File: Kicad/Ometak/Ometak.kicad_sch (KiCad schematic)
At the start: 26 parts, among them J1 Conn_01x02_Pin, J2 Conn_01x02_Pin, J3 Conn_01x02_Pin, Q1 IRF7303, U1 L7805, U2 PIC16F15214-I/SN, U3 LM358

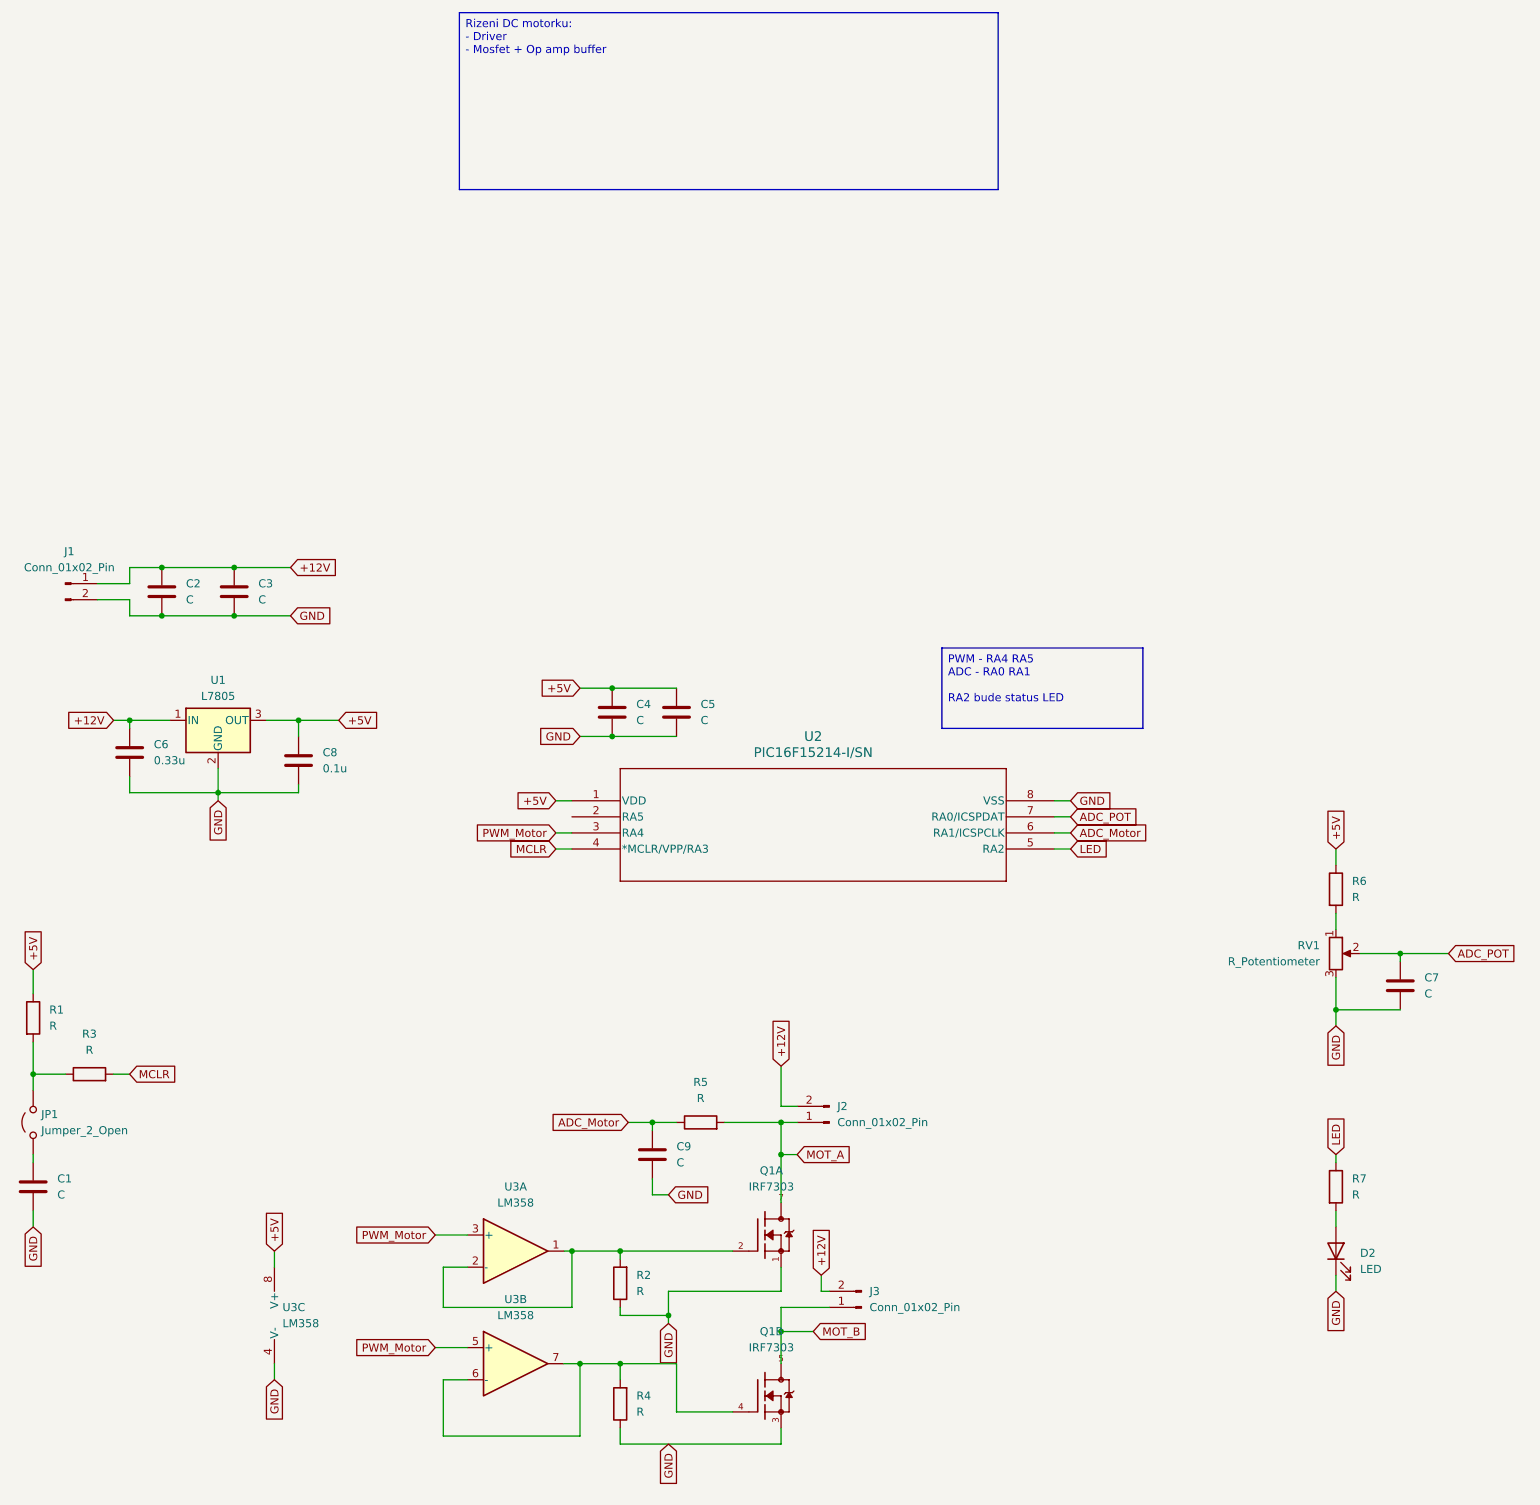
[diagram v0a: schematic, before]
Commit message: Pokrocilejsi verze ometaku - navrh
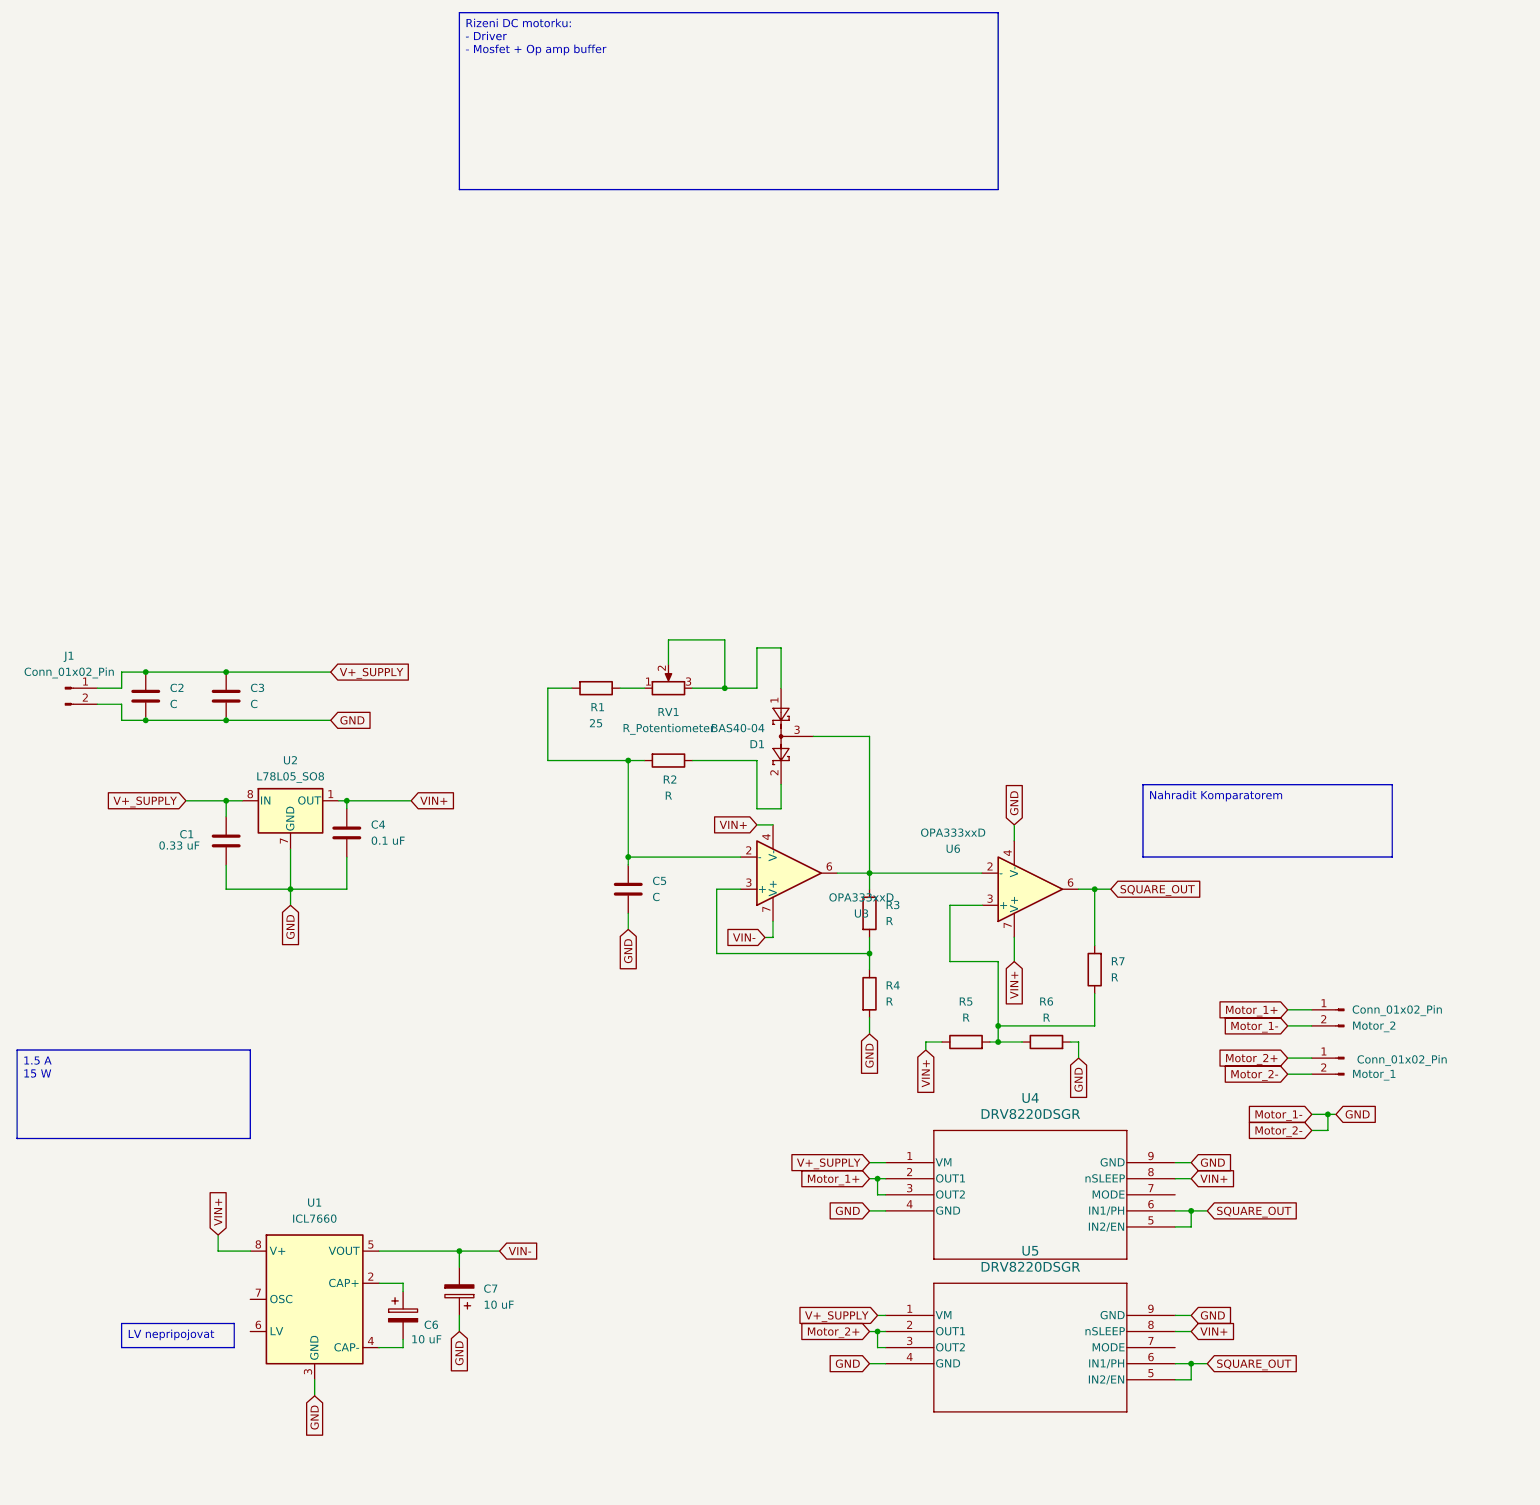
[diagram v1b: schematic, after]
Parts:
- removed C6: 0.33u, Capacitor_SMD:C_1206_3216Metric, symbol Device:C
- removed C7: C, Capacitor_SMD:C_0603_1608Metric, symbol Device:C
- removed C8: 0.1u, Capacitor_SMD:C_1206_3216Metric, symbol Device:C
- removed C9: C, symbol Device:C
- removed D2: LED, LED_SMD:LED_0603_1608Metric, symbol Device:LED
- removed J2, J3: Conn_01x02_Pin, Connector_PinHeader_2.54mm:PinHeader_1x02_P2.54mm_Vertical, symbol Connector:Conn_01x02_Pin
- removed JP1: Jumper_2_Open, Connector_PinHeader_1.27mm:PinHeader_1x02_P1.27mm_Vertical, symbol Jumper:Jumper_2_Open
- removed Q1: IRF7303, IRF7303:SOIC-8, symbol IRF7303:IRF7303
- removed U1: L7805, Package_TO_SOT_SMD:TO-252-2, symbol Regulator_Linear:L7805
- removed U2: PIC16F15214-I/SN, PIC16F15214:SOIC8_SN_MCH, symbol PIC16F15214:PIC16F15214-I_SN
- removed U3: LM358, Package_SO:SOIC-8_3.9x4.9mm_P1.27mm, symbol Amplifier_Operational:LM358
- added C6, C7: 10 uF, Capacitor_SMD:C_1206_3216Metric, symbol Device:C_Polarized
- added D1: BAS40-04, Package_TO_SOT_SMD:SOT-23, symbol Diode:BAS40-04
- added Motor_1, Motor_2: Conn_01x02_Pin, TerminalBlock:TerminalBlock_MaiXu_MX126-5.0-02P_1x02_P5.00mm, symbol Connector:Conn_01x02_Pin
- added U1: ICL7660, Package_SO:SOIC-8_3.9x4.9mm_P1.27mm, symbol Regulator_SwitchedCapacitor:ICL7660
- added U2: L78L05_SO8, Package_SO:SOIC-8_3.9x4.9mm_P1.27mm, symbol Regulator_Linear:L78L05_SO8
- added U3, U6: OPA333xxD, Package_SO:SOIC-8_3.9x4.9mm_P1.27mm, symbol Amplifier_Operational:OPA333xxD
- added U4, U5: DRV8220DSGR, WSON8_DSG_TEX, symbol DRV8220:DRV8220DSGR
- C1: value C -> 0.33 uF; footprint Capacitor_SMD:C_0603_1608Metric -> Capacitor_SMD:C_1206_3216Metric
- C2, C3: footprint Capacitor_THT:CP_Radial_D10.0mm_P2.50mm -> Capacitor_THT:CP_Radial_D10.0mm_P5.00mm
- C4: value C -> 0.1 uF; footprint Capacitor_SMD:C_0603_1608Metric -> Capacitor_SMD:C_1206_3216Metric
- C5: footprint Capacitor_SMD:C_0603_1608Metric -> Capacitor_SMD:C_1206_3216Metric
- J1: footprint Connector_PinHeader_2.54mm:PinHeader_1x02_P2.54mm_Vertical -> TerminalBlock:TerminalBlock_MaiXu_MX126-5.0-02P_1x02_P5.00mm
- R1: value R -> 25; footprint Resistor_SMD:R_0603_1608Metric -> Resistor_SMD:R_1206_3216Metric
- R3, R7: footprint Resistor_SMD:R_0603_1608Metric -> Resistor_SMD:R_1206_3216Metric
- R5: footprint (none) -> Resistor_SMD:R_1206_3216Metric
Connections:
- net +12V is gone; now on net V+_SUPPLY: C2.1, C3.1, J1.1 (Pin_1)
- net MOT_A is gone; now on an unnamed net: R5.2
- net GND: now also R4.2, R6.2, C7.1, Motor_1.2 (Pin_2), Motor_2.2 (Pin_2), U1.3 (GND), U2.2 (GND), U2.3 (GND), U2.6 (GND), U2.7 (GND), U4.4 (GND), U4.9 (GND), U5.4 (GND), U5.9 (GND), U6.4 (V-); no longer R2.1, R4.1, RV1.3
- net at R2.2: now also C5.1, R1.2, U3.2 (-)
- net at RV1.1: now also R1.1; no longer R6.2
- net V+_SUPPLY: now reaches C1.1
- net V+_SUPPLY: now also U2.8 (IN), U4.1 (VM), U5.1 (VM)
- net at R3.1: now also D1.3, U3.6, U6.2 (-); no longer R1.2
- net SQUARE_OUT: now reaches R7.2
- net SQUARE_OUT: now also U4.5 (IN2/EN), U4.6 (IN1/PH), U5.5 (IN2/EN), U5.6 (IN1/PH), U6.6
- removed net +5V: C4.1, C5.1, R1.1, R6.1
- net ADC_Motor renamed VIN+
- net VIN+: now also C4.1, U1.8 (V+), U2.1 (OUT), U3.4 (V-), U4.8 (nSLEEP), U5.8 (nSLEEP), U6.7 (V+)
- net ADC_POT: no longer names the net of RV1.2
- net ADC_POT: now also RV1.3, D1.1
- net LED: no longer names the net of R7.1
- net LED: now also R6.1, U6.3 (+)
- net MCLR: no longer names the net of R3.2
- net MCLR: now also R4.1, U3.3 (+)
- new net: D1.2, R2.1
- new net: C6.1, U1.2 (CAP+)
- new net: C6.2, U1.4 (CAP-)
- new net Motor_1+: Motor_2.1 (Pin_1), U4.2 (OUT1), U4.3 (OUT2)
- new net Motor_2+: Motor_1.1 (Pin_1), U5.2 (OUT1), U5.3 (OUT2)
- new net VIN-: C7.2, U1.5 (VOUT), U3.7 (V+)
